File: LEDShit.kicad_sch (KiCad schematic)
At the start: 71 parts

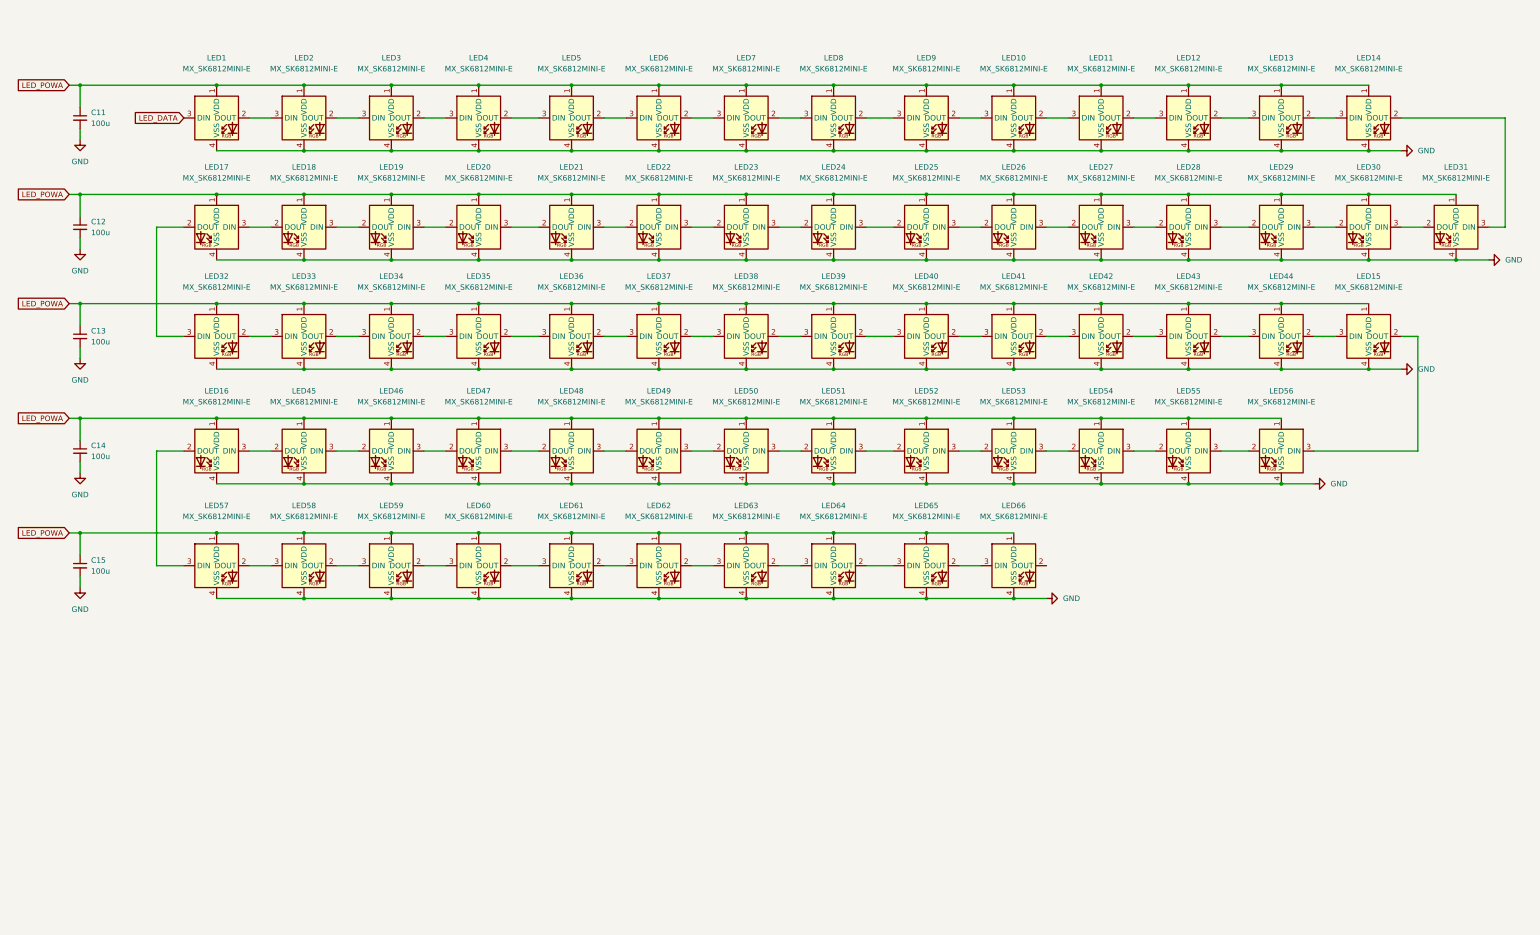
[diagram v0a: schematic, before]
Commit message: Finished LED matrix
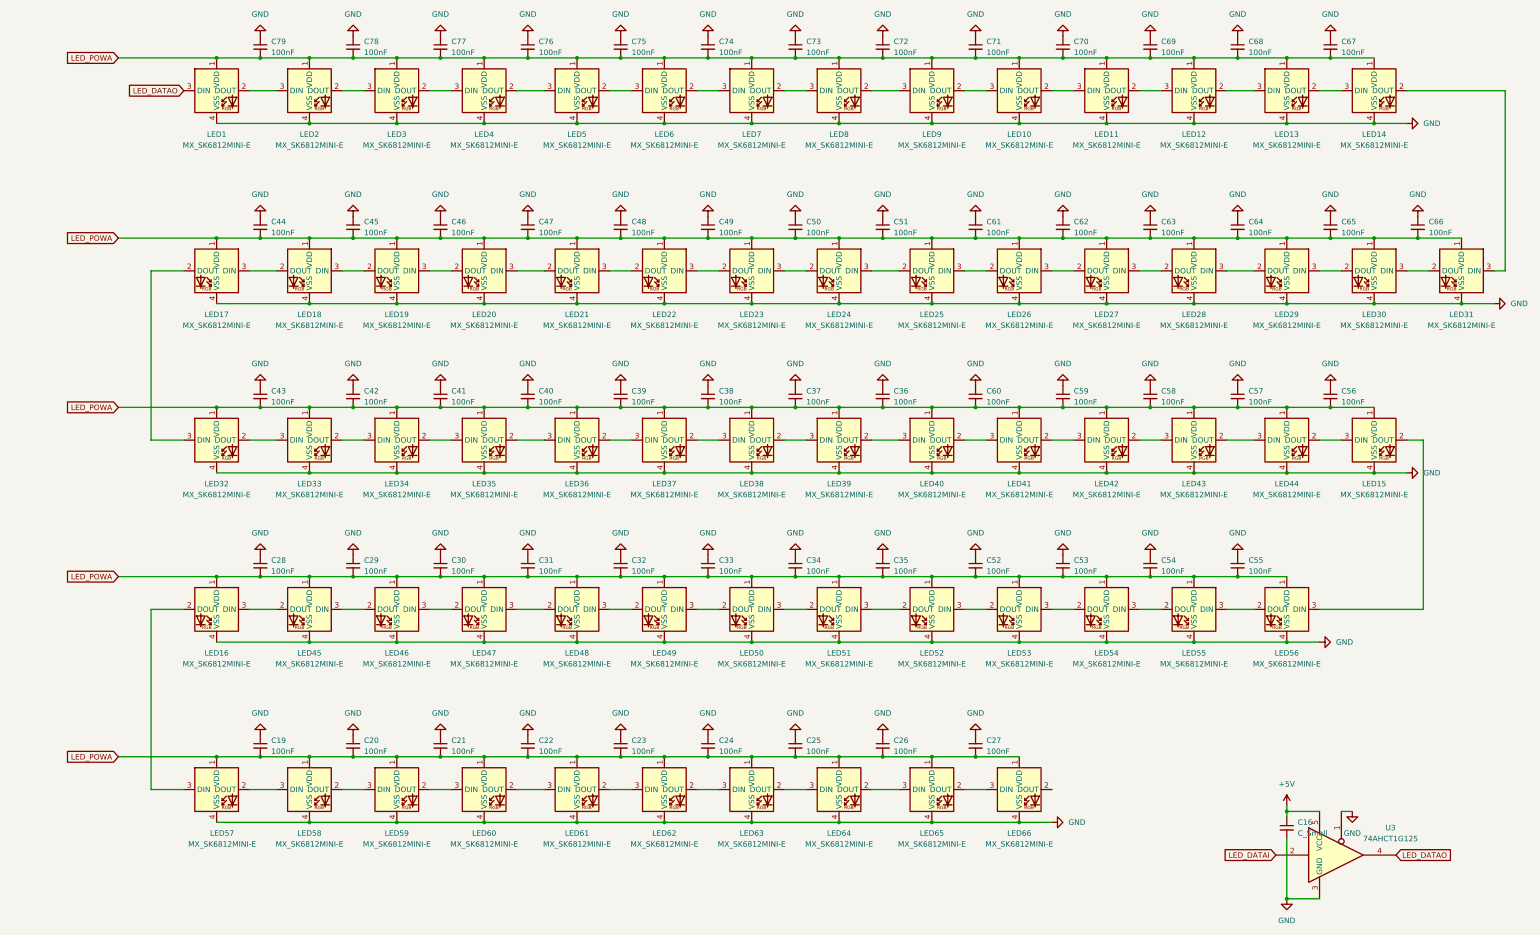
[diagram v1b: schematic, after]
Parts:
- removed C11, C12, C13, C14, C15: 100u, symbol Device:C_Small
- added C16: C_Small, symbol Device:C_Small
- added C19, C20, C21, C22, C23, C24, C25, C26, C27, C28, C29, C30, C31, C32, C33, C34, C35, C36, C37, C38, C39, C40, C41, C42, C43, C44, C45, C46, C47, C48, C49, C50, C51, C52, C53, C54, C55, C56, C57, C58, C59, C60, C61, C62, C63, C64, C65, C66, C67, C68, C69, C70, C71, C72, C73, C74, C75, C76, C77, C78, C79: 100nF, symbol Device:C_Small
- added U3: 74AHCT1G125, symbol 74xGxx:74AHCT1G125
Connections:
- net GND: now also C16.2, C19.1, C20.1, C21.1, C22.1, C23.1, C24.1, C25.1, C26.1, C27.1, C28.1, C29.1, C30.1, C31.1, C32.1, C33.1, C34.1, C35.1, C36.1, C37.1, C38.1, C39.1, C40.1, C41.1, C42.1, C43.1, C44.1, C45.1, C46.1, C47.1, C48.1, C49.1, C50.1, C51.1, C52.1, C53.1, C54.1, C55.1, C56.1, C57.1, C58.1, C59.1, C60.1, C61.1, C62.1, C63.1, C64.1, C65.1, C66.1, C67.1, C68.1, C69.1, C70.1, C71.1, C72.1, C73.1, C74.1, C75.1, C76.1, C77.1, C78.1, C79.1, U3.1, U3.3 (GND)
- net LED_POWA: now also C19.2, C20.2, C21.2, C22.2, C23.2, C24.2, C25.2, C26.2, C27.2, C28.2, C29.2, C30.2, C31.2, C32.2, C33.2, C34.2, C35.2, C36.2, C37.2, C38.2, C39.2, C40.2, C41.2, C42.2, C43.2, C44.2, C45.2, C46.2, C47.2, C48.2, C49.2, C50.2, C51.2, C52.2, C53.2, C54.2, C55.2, C56.2, C57.2, C58.2, C59.2, C60.2, C61.2, C62.2, C63.2, C64.2, C65.2, C66.2, C67.2, C68.2, C69.2, C70.2, C71.2, C72.2, C73.2, C74.2, C75.2, C76.2, C77.2, C78.2, C79.2
- net LED_DATA renamed LED_DATAO
- net LED_DATAO: now also U3.4
- new net +5V: C16.1, U3.5 (VCC)
- new net LED_DATAI: U3.2
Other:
- moved on the sheet: LED1, LED10, LED11, LED12, LED13, LED14, LED15, LED16, LED17, LED18, LED19, LED2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

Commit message: assigned schema
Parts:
- added C11, C12, C13, C14, C15: 100nF, Capacitor_SMD:C_0402_1005Metric, symbol Device:C_Small
- C16: value C_Small -> 100nF; footprint (none) -> Capacitor_SMD:C_0402_1005Metric
- C19, C20, C21, C22, C23, C24, C25, C26, C27, C28, C29, C30, C31, C32, C33, C34, C35, C36, C37, C38, C39, C40, C41, C42, C43, C44, C45, C46, C47, C48, C49, C50, C51, C52, C53, C54, C55, C56, C57, C58, C59, C60, C61, C62, C63, C64, C65, C66, C67, C68, C69, C70, C71, C72, C73, C74, C75, C76, C77, C78, C79: footprint (none) -> Capacitor_SMD:C_0402_1005Metric
- U3: footprint (none) -> Package_TO_SOT_SMD:SOT-23-5
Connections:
- net GND: now also C11.1, C12.1, C13.1, C14.1, C15.1
- net LED_POWA: now also C11.2, C12.2, C13.2, C14.2, C15.2
- no-connect marks 0 -> 1

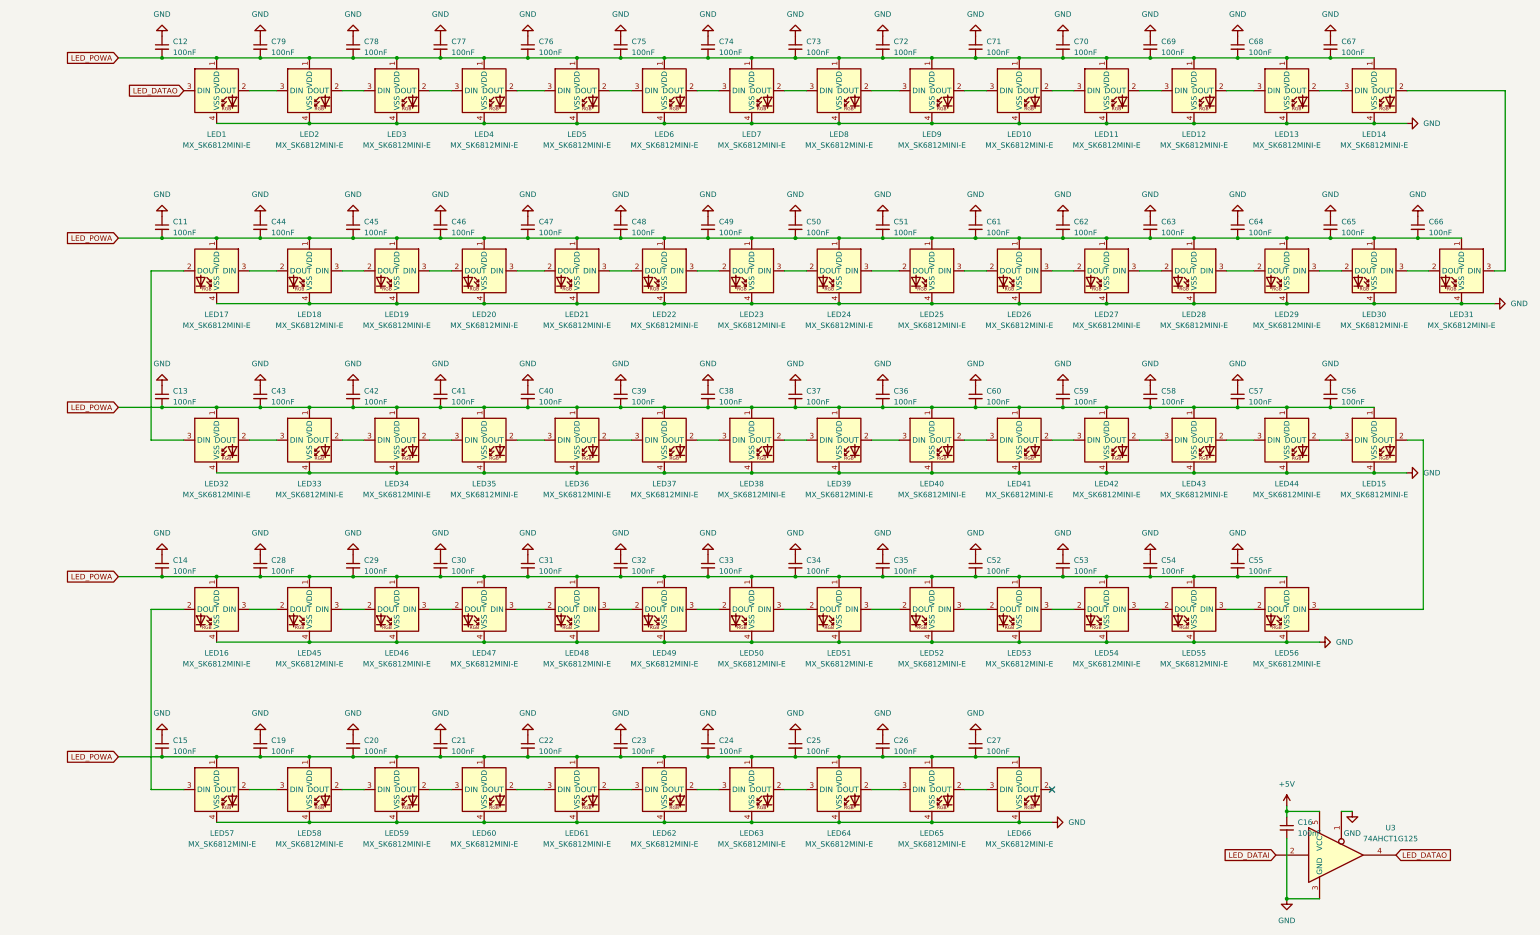
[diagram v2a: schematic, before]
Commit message: Fixes and routing
Routed Col and Row for switches.
Fixed annotation of LEDs and caps.
Started LED matrix Routing.
Started mcu and supporting routing.
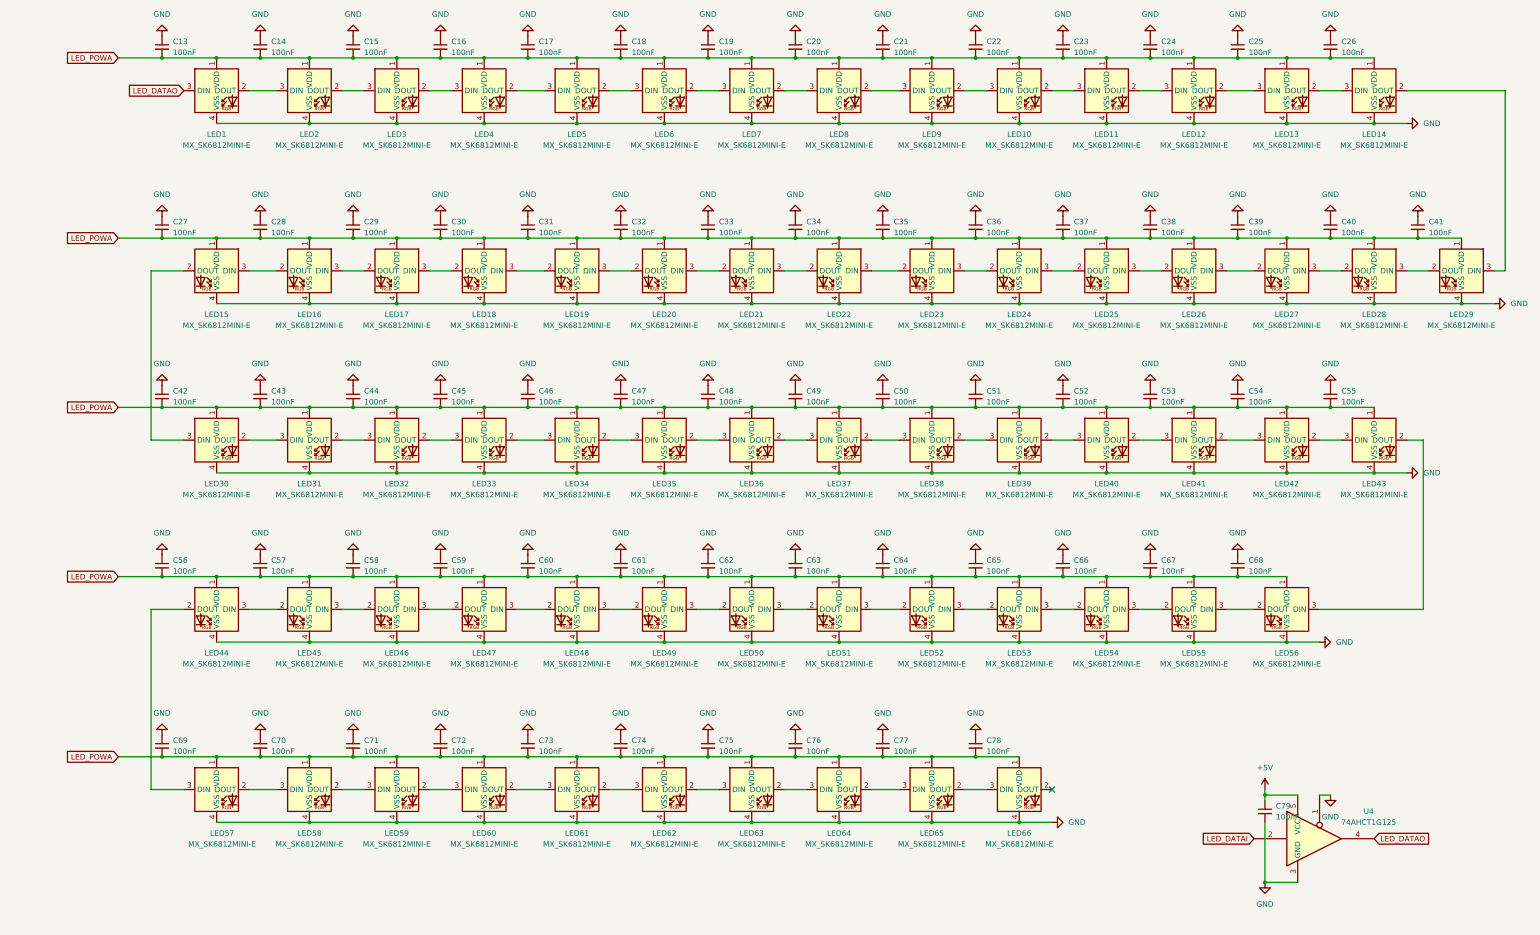
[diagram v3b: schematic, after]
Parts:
- removed C16: 100nF, Capacitor_SMD:C_0402_1005Metric, symbol Device:C_Small
- removed U3: 74AHCT1G125, Package_TO_SOT_SMD:SOT-23-5, symbol 74xGxx:74AHCT1G125
- added C79: 100nF, Capacitor_SMD:C_0402_1005Metric, symbol Device:C_Small
- added U4: 74AHCT1G125, Package_TO_SOT_SMD:SOT-23-5, symbol 74xGxx:74AHCT1G125
- renumbered C12 to C13, C79 to C14, C78 to C15, C77 to C16, C76 to C17, C75 to C18, C74 to C19, C73 to C20, C72 to C21, C71 to C22, C70 to C23, C69 to C24, C68 to C25, C67 to C26, C11 to C27, C44 to C28, C45 to C29, C46 to C30, C47 to C31, C48 to C32, C49 to C33, C50 to C34, C51 to C35, C61 to C36, C62 to C37, C63 to C38, C64 to C39, C65 to C40, C66 to C41, C13 to C42, C42 to C44, C41 to C45, C40 to C46, C39 to C47, C38 to C48, C37 to C49, C36 to C50, C60 to C51, C59 to C52, C58 to C53, C57 to C54, C56 to C55, C14 to C56, C28 to C57, C29 to C58, C30 to C59, C31 to C60, C32 to C61, C33 to C62, C34 to C63, C35 to C64, C52 to C65, C53 to C66, C54 to C67, C55 to C68, C15 to C69, C19 to C70, C20 to C71, C21 to C72, C22 to C73, C23 to C74, C24 to C75, C25 to C76, C26 to C77, C27 to C78, LED17 to LED15, LED18 to LED16, LED19 to LED17, LED20 to LED18, LED21 to LED19, LED22 to LED20, LED23 to LED21, LED24 to LED22, LED25 to LED23, LED26 to LED24, LED27 to LED25, LED28 to LED26, LED29 to LED27, LED30 to LED28, LED31 to LED29, LED32 to LED30, LED33 to LED31, LED34 to LED32, LED35 to LED33, LED36 to LED34, LED37 to LED35, LED38 to LED36, LED39 to LED37, LED40 to LED38, LED41 to LED39, LED42 to LED40, LED43 to LED41, LED44 to LED42, LED15 to LED43, LED16 to LED44
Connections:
- net +5V: now also C79.1, U4.5 (VCC)
- net GND: now also C79.2, U4.1, U4.3 (GND)
- net LED_DATAI: now also U4.2
- net LED_DATAO: now also U4.4

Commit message: Routing Done
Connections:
- net LED_POWA is gone; now on net +5V: C13.2, C14.2, C15.2, C16.2, C17.2, C18.2, C19.2, C20.2, C21.2, C22.2, C23.2, C24.2, C25.2, C26.2, C27.2, C28.2, C29.2, C30.2, C31.2, C32.2, C33.2, C34.2, C35.2, C36.2, C37.2, C38.2, C39.2, C40.2, C41.2, C42.2, C43.2, C44.2, C45.2, C46.2, C47.2, C48.2, C49.2, C50.2, C51.2, C52.2, C53.2, C54.2, C55.2, C56.2, C57.2, C58.2, C59.2, C60.2, C61.2, C62.2, C63.2, C64.2, C65.2, C66.2, C67.2, C68.2, C69.2, C70.2, C71.2, C72.2, C73.2, C74.2, C75.2, C76.2, C77.2, C78.2, LED1.1 (VDD), LED10.1 (VDD), LED11.1 (VDD), LED12.1 (VDD), LED13.1 (VDD), LED14.1 (VDD), LED15.1 (VDD), LED16.1 (VDD), LED17.1 (VDD), LED18.1 (VDD), LED19.1 (VDD), LED2.1 (VDD), LED20.1 (VDD), LED21.1 (VDD), LED22.1 (VDD), LED23.1 (VDD), LED24.1 (VDD), LED25.1 (VDD), LED26.1 (VDD), LED27.1 (VDD), LED28.1 (VDD), LED29.1 (VDD), LED3.1 (VDD), LED30.1 (VDD), LED31.1 (VDD), LED32.1 (VDD), LED33.1 (VDD), LED34.1 (VDD), LED35.1 (VDD), LED36.1 (VDD), LED37.1 (VDD), LED38.1 (VDD), LED39.1 (VDD), LED4.1 (VDD), LED40.1 (VDD), LED41.1 (VDD), LED42.1 (VDD), LED43.1 (VDD), LED44.1 (VDD), LED45.1 (VDD), LED46.1 (VDD), LED47.1 (VDD), LED48.1 (VDD), LED49.1 (VDD), LED5.1 (VDD), LED50.1 (VDD), LED51.1 (VDD), LED52.1 (VDD), LED53.1 (VDD), LED54.1 (VDD), LED55.1 (VDD), LED56.1 (VDD), LED57.1 (VDD), LED58.1 (VDD), LED59.1 (VDD), LED6.1 (VDD), LED60.1 (VDD), LED61.1 (VDD), LED62.1 (VDD), LED63.1 (VDD), LED64.1 (VDD), LED65.1 (VDD), LED66.1 (VDD), LED7.1 (VDD), LED8.1 (VDD), LED9.1 (VDD)
